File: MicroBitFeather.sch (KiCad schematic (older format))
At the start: 16 parts

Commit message: Decrease size of cap on 3.3V supply to 47uF.
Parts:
- C?: value 100uF -> 47uF; Description CAP ALUM 100UF 20% 10V RADIAL -> CAP ALUM 47UF 20% 16V RADIAL; Digi-Key_PN P963-ND -> P969-ND; MPN ECE-A1AKS101 -> ECE-A1CKS470
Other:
- note added: "Check\nconnector\ndiameter!"
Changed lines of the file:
@@
 P 7600 6350
 F 0 "C?" H 7625 6450 50  0000 L CNN
-F 1 "100uF" H 7625 6250 50  0000 L CNN
+F 1 "47uF" H 7625 6250 50  0000 L CNN
 F 2 "" H 7638 6200 50  0001 C CNN
 F 3 "" H 7600 6350 50  0001 C CNN
-F 4 "ECE-A1AKS101" H 7600 6350 60  0001 C CNN "MPN"
-F 5 "CAP ALUM 100UF 20% 10V RADIAL" H 7600 6350 60  0001 C CNN "Description"
-F 6 "P963-ND" H 7600 6350 60  0001 C CNN "Digi-Key_PN"
+F 4 "ECE-A1CKS470" H 7600 6350 60  0001 C CNN "MPN"
+F 5 "CAP ALUM 47UF 20% 16V RADIAL" H 7600 6350 60  0001 C CNN "Description"
+F 6 "P969-ND" H 7600 6350 60  0001 C CNN "Digi-Key_PN"
 	1    7600 6350
 	1    0    0    -1
@@
 	0    1    1    0
 $EndComp
+Text Notes 3800 6350 0    60   ~ 0
+Check\nconnector\ndiameter!
 $EndSCHEMATC

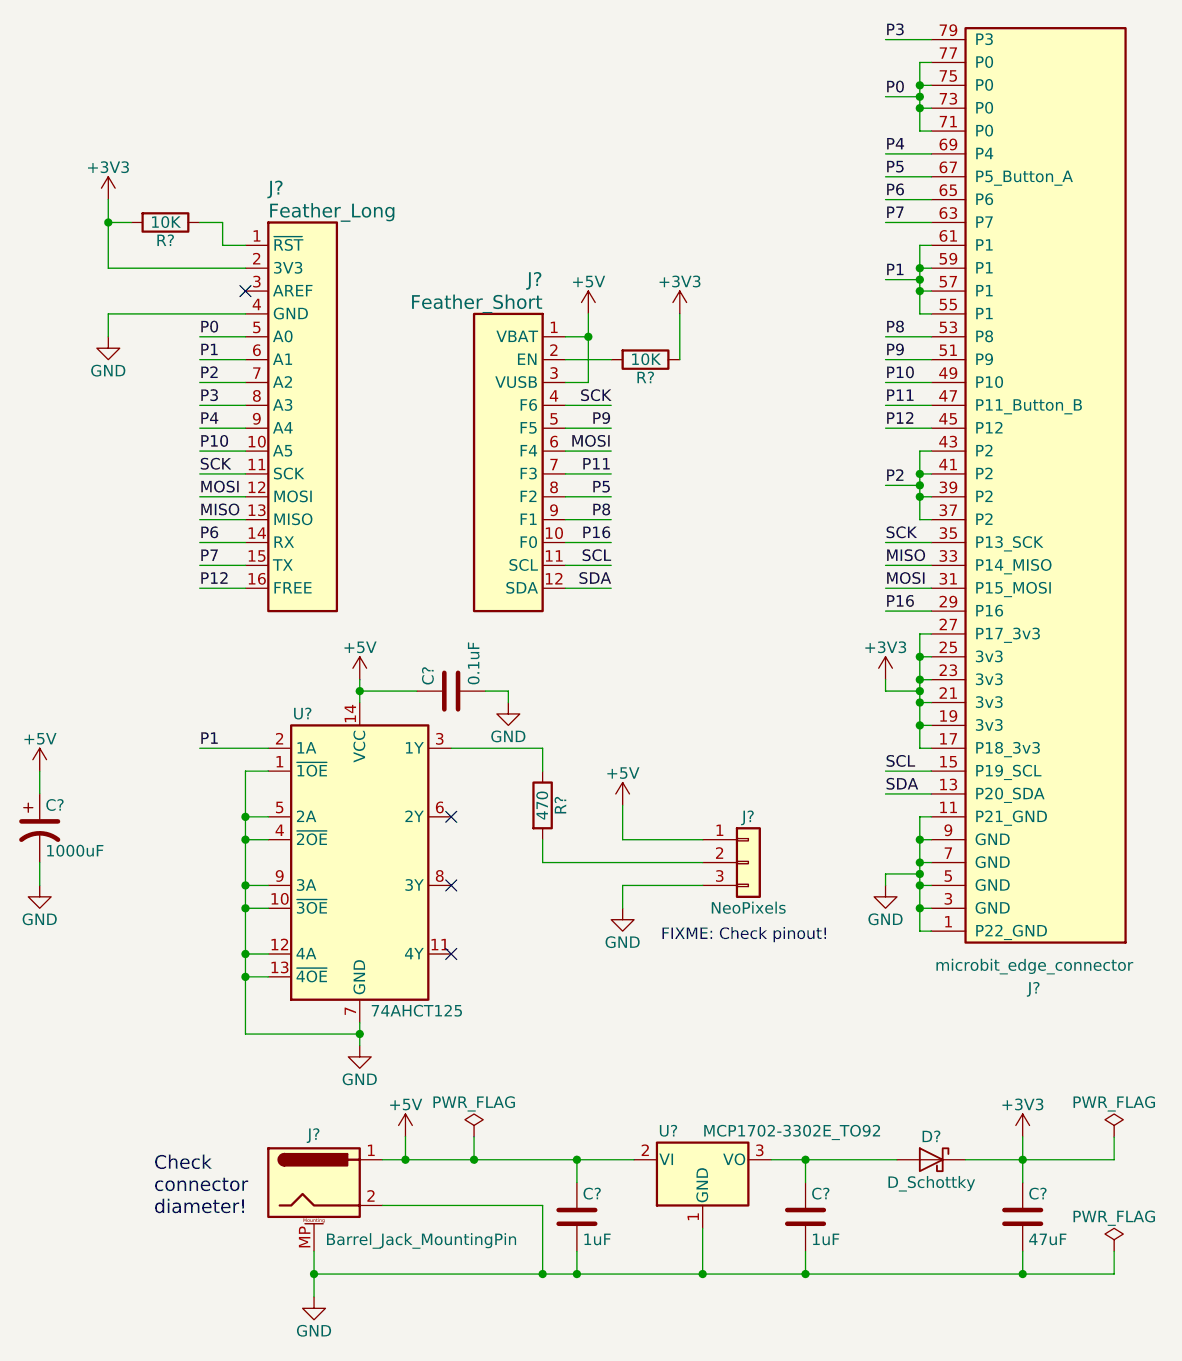
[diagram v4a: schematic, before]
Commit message: Use correct symbol for microfarads.
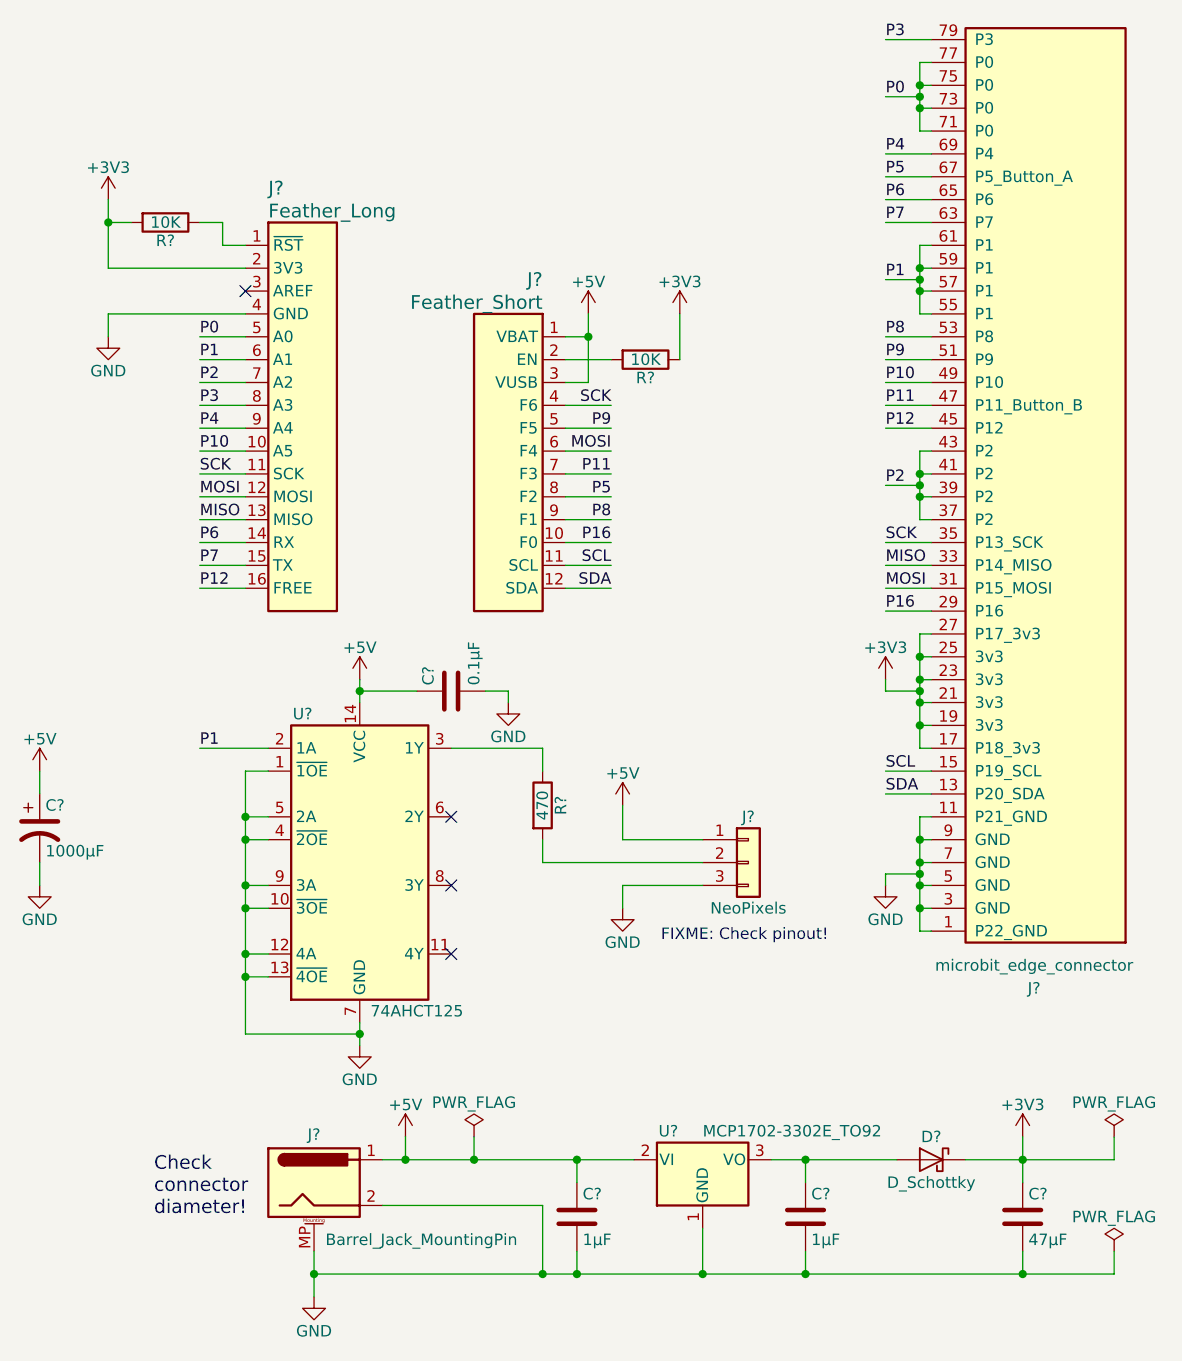
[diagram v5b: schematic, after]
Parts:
- C? (x2): value 1uF -> 1µF
- C?: value 47uF -> 47µF
- C?: value 0.1uF -> 0.1µF
- C?: value 1000uF -> 1000µF
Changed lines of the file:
@@
 P 5650 6350
 F 0 "C?" H 5675 6450 50  0000 L CNN
-F 1 "1uF" H 5675 6250 50  0000 L CNN
+F 1 "1µF" H 5675 6250 50  0000 L CNN
 F 2 "" H 5688 6200 50  0001 C CNN
 F 3 "" H 5650 6350 50  0001 C CNN
@@
 P 7600 6350
 F 0 "C?" H 7625 6450 50  0000 L CNN
-F 1 "47uF" H 7625 6250 50  0000 L CNN
+F 1 "47µF" H 7625 6250 50  0000 L CNN
 F 2 "" H 7638 6200 50  0001 C CNN
 F 3 "" H 7600 6350 50  0001 C CNN
@@
 P 5100 4050
 F 0 "C?" H 5125 4150 50  0000 L CNN
-F 1 "0.1uF" H 5125 3950 50  0000 L CNN
+F 1 "0.1µF" H 5125 3950 50  0000 L CNN
 F 2 "" H 5138 3900 50  0001 C CNN
 F 3 "" H 5100 4050 50  0001 C CNN
@@
 P 3300 4650
 F 0 "C?" H 3325 4750 50  0000 L CNN
-F 1 "1000uF" H 3325 4550 50  0000 L CNN
+F 1 "1000µF" H 3325 4550 50  0000 L CNN
 F 2 "" H 3300 4650 50  0001 C CNN
 F 3 "" H 3300 4650 50  0001 C CNN
@@
 P 6650 6350
 F 0 "C?" H 6675 6450 50  0000 L CNN
-F 1 "1uF" H 6675 6250 50  0000 L CNN
+F 1 "1µF" H 6675 6250 50  0000 L CNN
 F 2 "" H 6688 6200 50  0001 C CNN
 F 3 "" H 6650 6350 50  0001 C CNN

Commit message: Annotate components.
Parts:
- C5: renamed from C?; symbol C -> CP1
- gave numbers to parts that had none: 15
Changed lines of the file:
@@
 Sheet 1 1
 Title "Neopixel and FeatherWing adapter for Micro:Bit"
-Date ""
+Date "2017-08-30"
 Rev ""
 Comp "Patrick Pelletier"
@@
 $EndDescr
 $Comp
-L microbit_edge_connector J?
+L microbit_edge_connector J5
 U 1 1 5B875D43
 P 7700 3300
-F 0 "J?" H 7750 5350 50  0000 C CNN
+F 0 "J5" H 7750 5350 50  0000 C CNN
 F 1 "microbit_edge_connector" H 7750 5250 50  0000 C CNN
 F 2 "" H 7600 3200 50  0001 C CNN
@@
 $EndComp
 $Comp
-L Feather_Long J?
+L Feather_Long J1
 U 1 1 5B875D68
 P 4200 2100
-F 0 "J?" H 4300 2350 60  0000 L CNN
+F 0 "J1" H 4300 2350 60  0000 L CNN
 F 1 "Feather_Long" H 4300 2250 60  0000 L CNN
 F 2 "" H 4200 2100 60  0001 C CNN
@@
 $EndComp
 $Comp
-L Feather_Short J?
+L Feather_Short J3
 U 1 1 5B875D93
 P 5600 2500
-F 0 "J?" H 5700 2750 60  0000 L CNN
+F 0 "J3" H 5700 2750 60  0000 L CNN
 F 1 "Feather_Short" H 5700 2650 60  0000 L CNN
 F 2 "" H 5600 2500 60  0001 C CNN
@@
 Connection ~ 7150 4200
 $Comp
-L +3V3 #PWR?
+L +3V3 #PWR14
 U 1 1 5B877C6E
 P 7000 4000
-F 0 "#PWR?" H 7000 3850 50  0001 C CNN
+F 0 "#PWR14" H 7000 3850 50  0001 C CNN
 F 1 "+3V3" H 7000 4140 50  0000 C CNN
 F 2 "" H 7000 4000 50  0001 C CNN
@@
 Connection ~ 7150 5000
 $Comp
-L GND #PWR?
+L GND #PWR15
 U 1 1 5B877F3E
 P 7000 4900
-F 0 "#PWR?" H 7000 4650 50  0001 C CNN
+F 0 "#PWR15" H 7000 4650 50  0001 C CNN
 F 1 "GND" H 7000 4750 50  0000 C CNN
 F 2 "" H 7000 4900 50  0001 C CNN
@@
 Connection ~ 7150 4850
 $Comp
-L R R?
+L R R1
 U 1 1 5B87813D
 P 3850 2000
-F 0 "R?" V 3930 2000 50  0000 C CNN
+F 0 "R1" V 3930 2000 50  0000 C CNN
 F 1 "10K" V 3850 2000 50  0000 C CNN
 F 2 "" V 3780 2000 50  0001 C CNN
@@
 $EndComp
 $Comp
-L +3V3 #PWR?
+L +3V3 #PWR3
 U 1 1 5B87818E
 P 3600 1900
-F 0 "#PWR?" H 3600 1750 50  0001 C CNN
+F 0 "#PWR3" H 3600 1750 50  0001 C CNN
 F 1 "+3V3" H 3600 2040 50  0000 C CNN
 F 2 "" H 3600 1900 50  0001 C CNN
@@
 NoConn ~ 4200 2300
 $Comp
-L GND #PWR?
+L GND #PWR4
 U 1 1 5B878369
 P 3600 2500
-F 0 "#PWR?" H 3600 2250 50  0001 C CNN
+F 0 "#PWR4" H 3600 2250 50  0001 C CNN
 F 1 "GND" H 3600 2350 50  0000 C CNN
 F 2 "" H 3600 2500 50  0001 C CNN
@@
 	4000 3600 4200 3600
 $Comp
-L +3V3 #PWR?
+L +3V3 #PWR13
 U 1 1 5B878A64
 P 6100 2400
-F 0 "#PWR?" H 6100 2250 50  0001 C CNN
+F 0 "#PWR13" H 6100 2250 50  0001 C CNN
 F 1 "+3V3" H 6100 2540 50  0000 C CNN
 F 2 "" H 6100 2400 50  0001 C CNN
@@
 	5600 2600 5800 2600
 $Comp
-L +5V #PWR?
+L +5V #PWR10
 U 1 1 5B878BFE
 P 5700 2400
-F 0 "#PWR?" H 5700 2250 50  0001 C CNN
+F 0 "#PWR10" H 5700 2250 50  0001 C CNN
 F 1 "+5V" H 5700 2540 50  0000 C CNN
 F 2 "" H 5700 2400 50  0001 C CNN
@@
 	5600 3600 5800 3600
 $Comp
-L Conn_01x03 J?
+L Conn_01x03 J4
 U 1 1 5B8792D8
 P 6400 4800
-F 0 "J?" H 6400 5000 50  0000 C CNN
+F 0 "J4" H 6400 5000 50  0000 C CNN
 F 1 "NeoPixels" H 6400 4600 50  0000 C CNN
 F 2 "" H 6400 4800 50  0001 C CNN
@@
 FIXME: Check pinout!
 $Comp
-L GND #PWR?
+L GND #PWR12
 U 1 1 5B87949E
 P 5850 5000
-F 0 "#PWR?" H 5850 4750 50  0001 C CNN
+F 0 "#PWR12" H 5850 4750 50  0001 C CNN
 F 1 "GND" H 5850 4850 50  0000 C CNN
 F 2 "" H 5850 5000 50  0001 C CNN
@@
 $EndComp
 $Comp
-L +5V #PWR?
+L +5V #PWR11
 U 1 1 5B8794C4
 P 5850 4550
-F 0 "#PWR?" H 5850 4400 50  0001 C CNN
+F 0 "#PWR11" H 5850 4400 50  0001 C CNN
 F 1 "+5V" H 5850 4690 50  0000 C CNN
 F 2 "" H 5850 4550 50  0001 C CNN
@@
 	5850 4900 6200 4900
 $Comp
-L 74AHCT125 U?
+L 74AHCT125 U1
 U 1 1 5B8786B5
 P 4700 4800
-F 0 "U?" H 4450 5450 50  0000 C CNN
+F 0 "U1" H 4450 5450 50  0000 C CNN
 F 1 "74AHCT125" H 4950 4150 50  0000 C CNN
 F 2 "" H 4700 4800 60  0000 C CNN
@@
 $EndComp
 $Comp
-L Barrel_Jack_MountingPin J?
+L Barrel_Jack_MountingPin J2
 U 1 1 5B8786E0
 P 4500 6200
-F 0 "J?" H 4500 6410 50  0000 C CNN
+F 0 "J2" H 4500 6410 50  0000 C CNN
 F 1 "Barrel_Jack_MountingPin" H 4550 5950 50  0000 L CNN
 F 2 "" H 4550 6160 50  0001 C CNN
@@
 $EndComp
 $Comp
-L +5V #PWR?
+L +5V #PWR6
 U 1 1 5B87920C
 P 4700 4000
-F 0 "#PWR?" H 4700 3850 50  0001 C CNN
+F 0 "#PWR6" H 4700 3850 50  0001 C CNN
 F 1 "+5V" H 4700 4140 50  0000 C CNN
 F 2 "" H 4700 4000 50  0001 C CNN
@@
 $EndComp
 $Comp
-L GND #PWR?
+L GND #PWR7
 U 1 1 5B879238
 P 4700 5600
-F 0 "#PWR?" H 4700 5350 50  0001 C CNN
+F 0 "#PWR7" H 4700 5350 50  0001 C CNN
 F 1 "GND" H 4700 5450 50  0000 C CNN
 F 2 "" H 4700 5600 50  0001 C CNN
@@
 	4700 5500 4700 5600
 $Comp
-L +5V #PWR?
+L +5V #PWR8
 U 1 1 5B879F10
 P 4900 6000
-F 0 "#PWR?" H 4900 5850 50  0001 C CNN
+F 0 "#PWR8" H 4900 5850 50  0001 C CNN
 F 1 "+5V" H 4900 6140 50  0000 C CNN
 F 2 "" H 4900 6000 50  0001 C CNN
@@
 $EndComp
 $Comp
-L GND #PWR?
+L GND #PWR5
 U 1 1 5B879F3C
 P 4500 6700
-F 0 "#PWR?" H 4500 6450 50  0001 C CNN
+F 0 "#PWR5" H 4500 6450 50  0001 C CNN
 F 1 "GND" H 4500 6550 50  0000 C CNN
 F 2 "" H 4500 6700 50  0001 C CNN
@@
 NoConn ~ 5100 5200
 $Comp
-L R R?
+L R R2
 U 1 1 5B87B000
 P 5500 4550
-F 0 "R?" V 5580 4550 50  0000 C CNN
+F 0 "R2" V 5580 4550 50  0000 C CNN
 F 1 "470" V 5500 4550 50  0000 C CNN
 F 2 "" V 5430 4550 50  0001 C CNN
@@
 	5500 4700 5500 4800
 $Comp
-L MCP1700-3302E_TO92 U?
+L MCP1700-3302E_TO92 U2
 U 1 1 5B87B6E7
 P 6200 6100
-F 0 "U?" H 6050 5975 50  0000 C CNN
+F 0 "U2" H 6050 5975 50  0000 C CNN
 F 1 "MCP1702-3302E_TO92" H 6200 5975 50  0000 L CNN
 F 2 "TO_SOT_Packages_THT:TO-92_Inline_Narrow_Oval" H 6200 5900 50  0001 C CIN
@@
 $EndComp
 $Comp
-L C C?
+L C C3
 U 1 1 5B87B8CD
 P 5650 6350
-F 0 "C?" H 5675 6450 50  0000 L CNN
+F 0 "C3" H 5675 6450 50  0000 L CNN
 F 1 "1µF" H 5675 6250 50  0000 L CNN
 F 2 "" H 5688 6200 50  0001 C CNN
@@
 Connection ~ 6200 6600
 $Comp
-L +3V3 #PWR?
+L +3V3 #PWR16
 U 1 1 5B87BEFA
 P 7600 6000
-F 0 "#PWR?" H 7600 5850 50  0001 C CNN
+F 0 "#PWR16" H 7600 5850 50  0001 C CNN
 F 1 "+3V3" H 7600 6140 50  0000 C CNN
 F 2 "" H 7600 6000 50  0001 C CNN
@@
 	6650 6100 6650 6200
 $Comp
-L D_Schottky D?
+L D_Schottky D1
 U 1 1 5B87C03F
 P 7200 6100
-F 0 "D?" H 7200 6200 50  0000 C CNN
+F 0 "D1" H 7200 6200 50  0000 C CNN
 F 1 "D_Schottky" H 7200 6000 50  0000 C CNN
 F 2 "" H 7200 6100 50  0001 C CNN
@@
 	7600 6000 7600 6200
 $Comp
-L C C?
+L CP1 C5
 U 1 1 5B87C55E
 P 7600 6350
-F 0 "C?" H 7625 6450 50  0000 L CNN
+F 0 "C5" H 7625 6450 50  0000 L CNN
 F 1 "47µF" H 7625 6250 50  0000 L CNN
 F 2 "" H 7638 6200 50  0001 C CNN
@@
 Connection ~ 5650 6100
 $Comp
-L C C?
+L C C2
 U 1 1 5B87CADC
 P 5100 4050
-F 0 "C?" H 5125 4150 50  0000 L CNN
+F 0 "C2" H 5125 4150 50  0000 L CNN
 F 1 "0.1µF" H 5125 3950 50  0000 L CNN
 F 2 "" H 5138 3900 50  0001 C CNN
@@
 $EndComp
 $Comp
-L GND #PWR?
+L GND #PWR9
 U 1 1 5B87CC46
 P 5350 4100
-F 0 "#PWR?" H 5350 3850 50  0001 C CNN
+F 0 "#PWR9" H 5350 3850 50  0001 C CNN
 F 1 "GND" H 5350 3950 50  0000 C CNN
 F 2 "" H 5350 4100 50  0001 C CNN
@@
 	5350 4050 5350 4100
 $Comp
-L CP1 C?
+L CP1 C1
 U 1 1 5B87D36C
 P 3300 4650
-F 0 "C?" H 3325 4750 50  0000 L CNN
+F 0 "C1" H 3325 4750 50  0000 L CNN
 F 1 "1000µF" H 3325 4550 50  0000 L CNN
 F 2 "" H 3300 4650 50  0001 C CNN
@@
 $EndComp
 $Comp
-L GND #PWR?
+L GND #PWR2
 U 1 1 5B87D3B2
 P 3300 4900
-F 0 "#PWR?" H 3300 4650 50  0001 C CNN
+F 0 "#PWR2" H 3300 4650 50  0001 C CNN
 F 1 "GND" H 3300 4750 50  0000 C CNN
 F 2 "" H 3300 4900 50  0001 C CNN
@@
 $EndComp
 $Comp
-L +5V #PWR?
+L +5V #PWR1
 U 1 1 5B87D3F6
 P 3300 4400
-F 0 "#PWR?" H 3300 4250 50  0001 C CNN
+F 0 "#PWR1" H 3300 4250 50  0001 C CNN
 F 1 "+5V" H 3300 4540 50  0000 C CNN
 F 2 "" H 3300 4400 50  0001 C CNN
@@
 	3300 4800 3300 4900
 $Comp
-L PWR_FLAG #FLG?
+L PWR_FLAG #FLG1
 U 1 1 5B87DB70
 P 5200 6000
-F 0 "#FLG?" H 5200 6075 50  0001 C CNN
+F 0 "#FLG1" H 5200 6075 50  0001 C CNN
 F 1 "PWR_FLAG" H 5200 6150 50  0000 C CNN
 F 2 "" H 5200 6000 50  0001 C CNN
@@
 $EndComp
 $Comp
-L PWR_FLAG #FLG?
+L PWR_FLAG #FLG2
 U 1 1 5B87DBB4
 P 8000 6000
-F 0 "#FLG?" H 8000 6075 50  0001 C CNN
+F 0 "#FLG2" H 8000 6075 50  0001 C CNN
 F 1 "PWR_FLAG" H 8000 6150 50  0000 C CNN
 F 2 "" H 8000 6000 50  0001 C CNN
@@
 $EndComp
 $Comp
-L PWR_FLAG #FLG?
+L PWR_FLAG #FLG3
 U 1 1 5B87DBF8
 P 8000 6500
-F 0 "#FLG?" H 8000 6575 50  0001 C CNN
+F 0 "#FLG3" H 8000 6575 50  0001 C CNN
 F 1 "PWR_FLAG" H 8000 6650 50  0000 C CNN
 F 2 "" H 8000 6500 50  0001 C CNN
@@
 Connection ~ 7600 6600
 $Comp
-L C C?
+L C C4
 U 1 1 5B888051
 P 6650 6350
-F 0 "C?" H 6675 6450 50  0000 L CNN
+F 0 "C4" H 6675 6450 50  0000 L CNN
 F 1 "1µF" H 6675 6250 50  0000 L CNN
 F 2 "" H 6688 6200 50  0001 C CNN
@@
 $EndComp
 $Comp
-L R R?
+L R R3
 U 1 1 5B88A204
 P 5950 2600
-F 0 "R?" V 6030 2600 50  0000 C CNN
+F 0 "R3" V 6030 2600 50  0000 C CNN
 F 1 "10K" V 5950 2600 50  0000 C CNN
 F 2 "" V 5880 2600 50  0001 C CNN
